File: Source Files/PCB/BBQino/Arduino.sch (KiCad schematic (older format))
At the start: 1 part

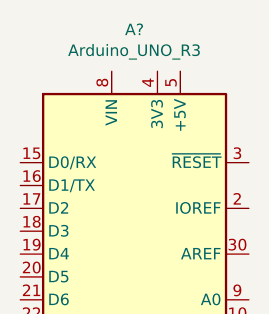
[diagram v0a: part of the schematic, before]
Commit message: 230V section first Draft. Added external module on top of the shield for the 230V section
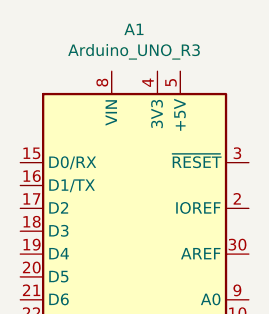
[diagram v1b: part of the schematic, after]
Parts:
- gave numbers to parts that had none: 1
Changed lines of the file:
@@
 $EndDescr
 $Comp
-L BBQino-rescue:Arduino_UNO_R3-MCU_Module A?
+L BBQino-rescue:Arduino_UNO_R3-MCU_Module A1
 U 1 1 613FC931
 P 2900 3200
-F 0 "A?" H 2900 4381 50  0000 C CNN
+F 0 "A1" H 2900 4381 50  0000 C CNN
 F 1 "Arduino_UNO_R3" H 2900 4290 50  0000 C CNN
 F 2 "Module:Arduino_UNO_R3_WithMountingHoles" H 2900 3200 50  0001 C CIN
@@
 $EndComp
 $Comp
-L BBQino-rescue:GNDD-power #PWR?
+L BBQino-rescue:GNDD-power #PWR0113
 U 1 1 6143AD0C
 P 3000 4400
-F 0 "#PWR?" H 3000 4150 50  0001 C CNN
+F 0 "#PWR0113" H 3000 4150 50  0001 C CNN
 F 1 "GNDD" H 3004 4245 50  0000 C CNN
 F 2 "" H 3000 4400 50  0001 C CNN

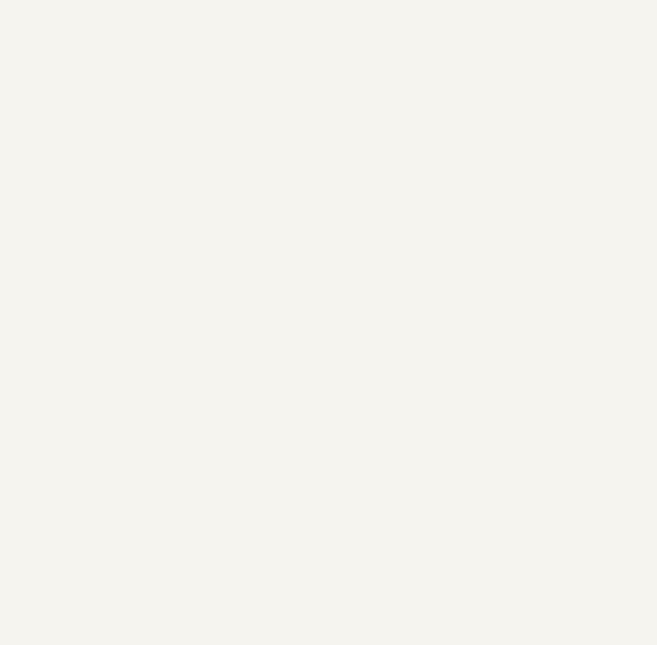
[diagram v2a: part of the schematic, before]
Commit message: added current sense on motor side
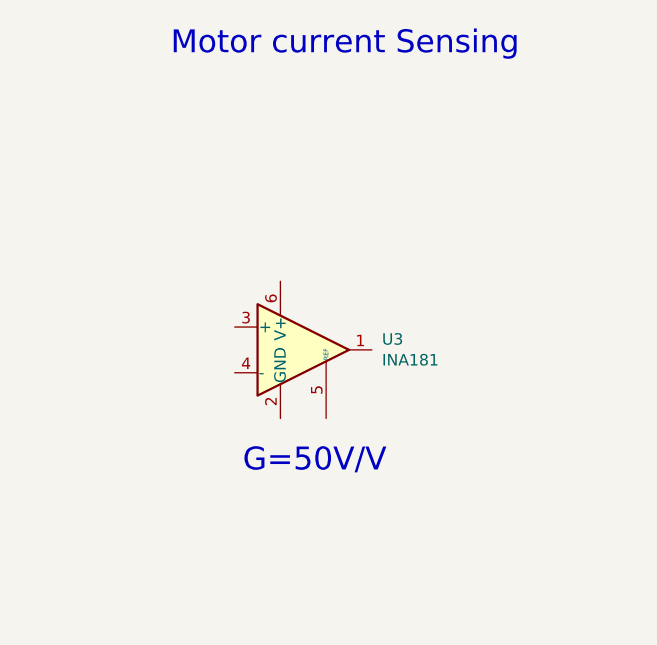
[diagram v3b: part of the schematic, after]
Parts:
- added U3: INA181, Package_TO_SOT_SMD:SOT-23-6, symbol Amplifier_Current:INA181
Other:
- note added: "G=50V/V\n"
- note added: "Motor current Sensing"
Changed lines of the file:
@@
 Wire Wire Line
 	2900 4400 3000 4400
+$Comp
+L Amplifier_Current:INA181 U?
+U 1 1 618CA589
+P 8780 2410
+AR Path="/613C1456/618CA589" Ref="U?"  Part="1"
+AR Path="/613FC6D4/618CA589" Ref="U3"  Part="1"
+F 0 "U3" H 9124 2456 50  0000 L CNN
+F 1 "INA181" H 9124 2365 50  0000 L CNN
+F 2 "Package_TO_SOT_SMD:SOT-23-6" H 8830 2460 50  0001 C CNN
+F 3 "http://www.ti.com/lit/ds/symlink/ina181.pdf" H 8930 2560 50  0001 C CNN
+	1    8780 2410
+	1    0    0    -1
+$EndComp
+Text Notes 8515 2955 0    100  ~ 0
+G=50V/V\n
+Text Notes 8200 1130 0    100  ~ 0
+Motor current Sensing
 $EndSCHEMATC

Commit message: New architecture
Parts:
- U3: symbol Amplifier_Current:INA181 -> BBQino-rescue:INA181-Amplifier_Current
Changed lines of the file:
@@
 $Descr A4 11693 8268
 encoding utf-8
-Sheet 4 6
+Sheet 4 7
 Title ""
 Date ""
@@
 	2900 4400 3000 4400
 $Comp
-L Amplifier_Current:INA181 U?
+L BBQino-rescue:INA181-Amplifier_Current U?
 U 1 1 618CA589
 P 8780 2410
 AR Path="/613C1456/618CA589" Ref="U?"  Part="1"
 AR Path="/613FC6D4/618CA589" Ref="U3"  Part="1"
+AR Path="/618CA589" Ref="U3"  Part="1"
 F 0 "U3" H 9124 2456 50  0000 L CNN
 F 1 "INA181" H 9124 2365 50  0000 L CNN
